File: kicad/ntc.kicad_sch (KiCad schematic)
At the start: 22 parts, among them J1 AudioJack2_SwitchT, J2 AudioJack2_SwitchT, J3 AudioJack2_SwitchT, J4 AudioJack2_SwitchT, J5 AudioJack2_SwitchT, J6 AudioJack2_SwitchT

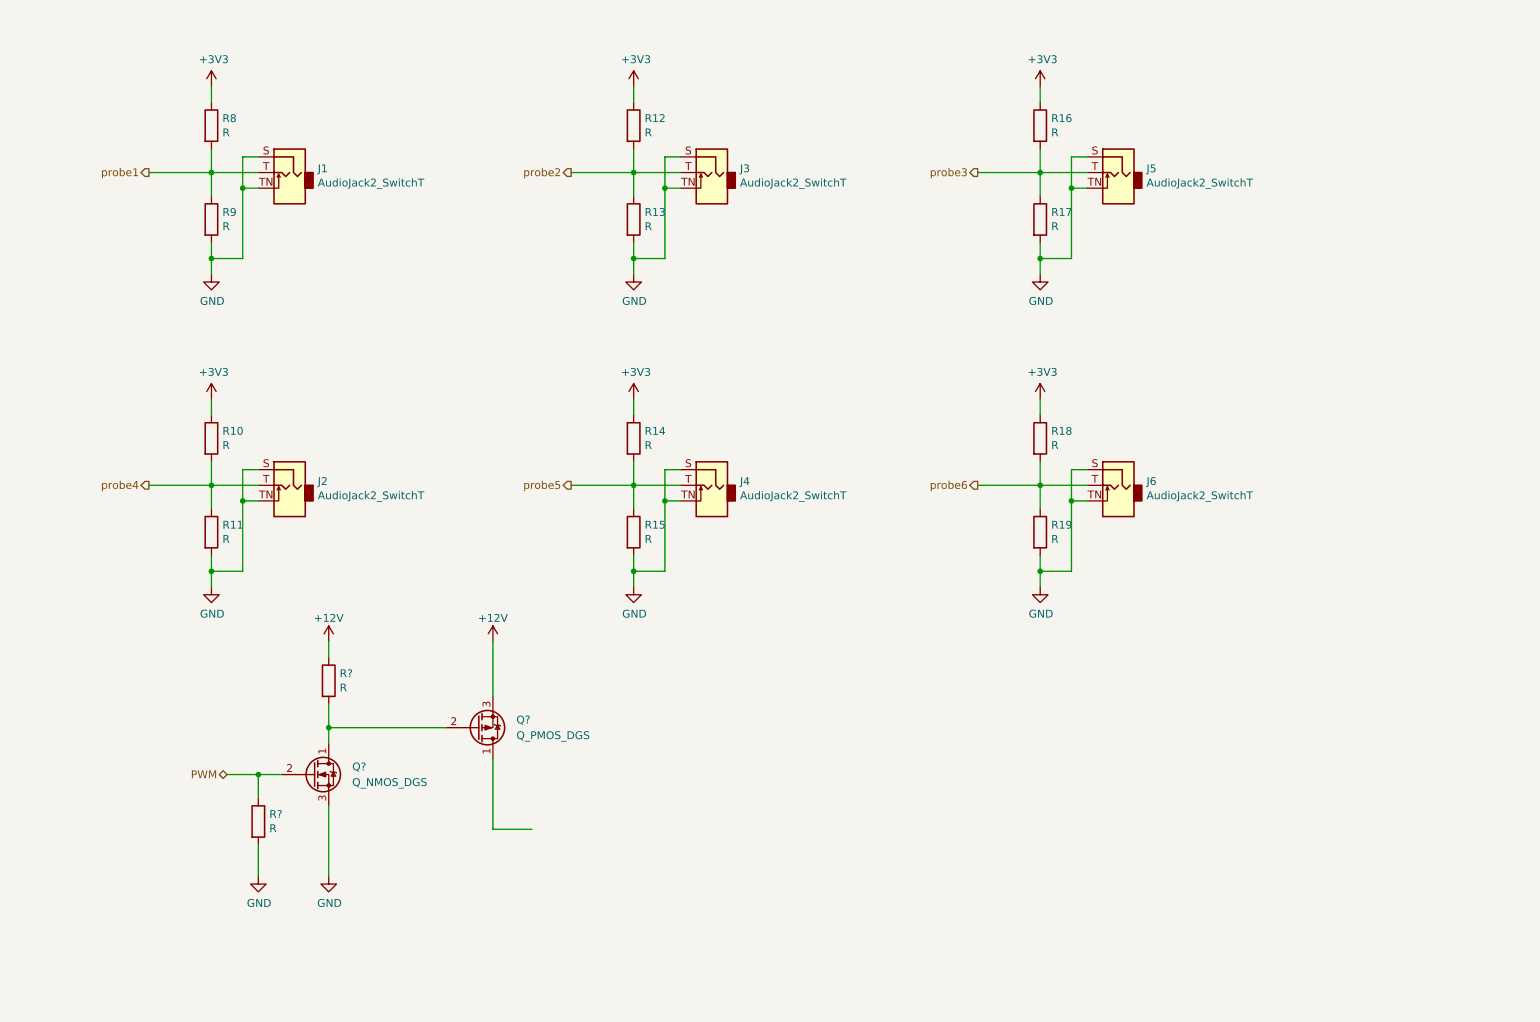
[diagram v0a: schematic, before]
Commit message: refactor KiCAD Project to v6
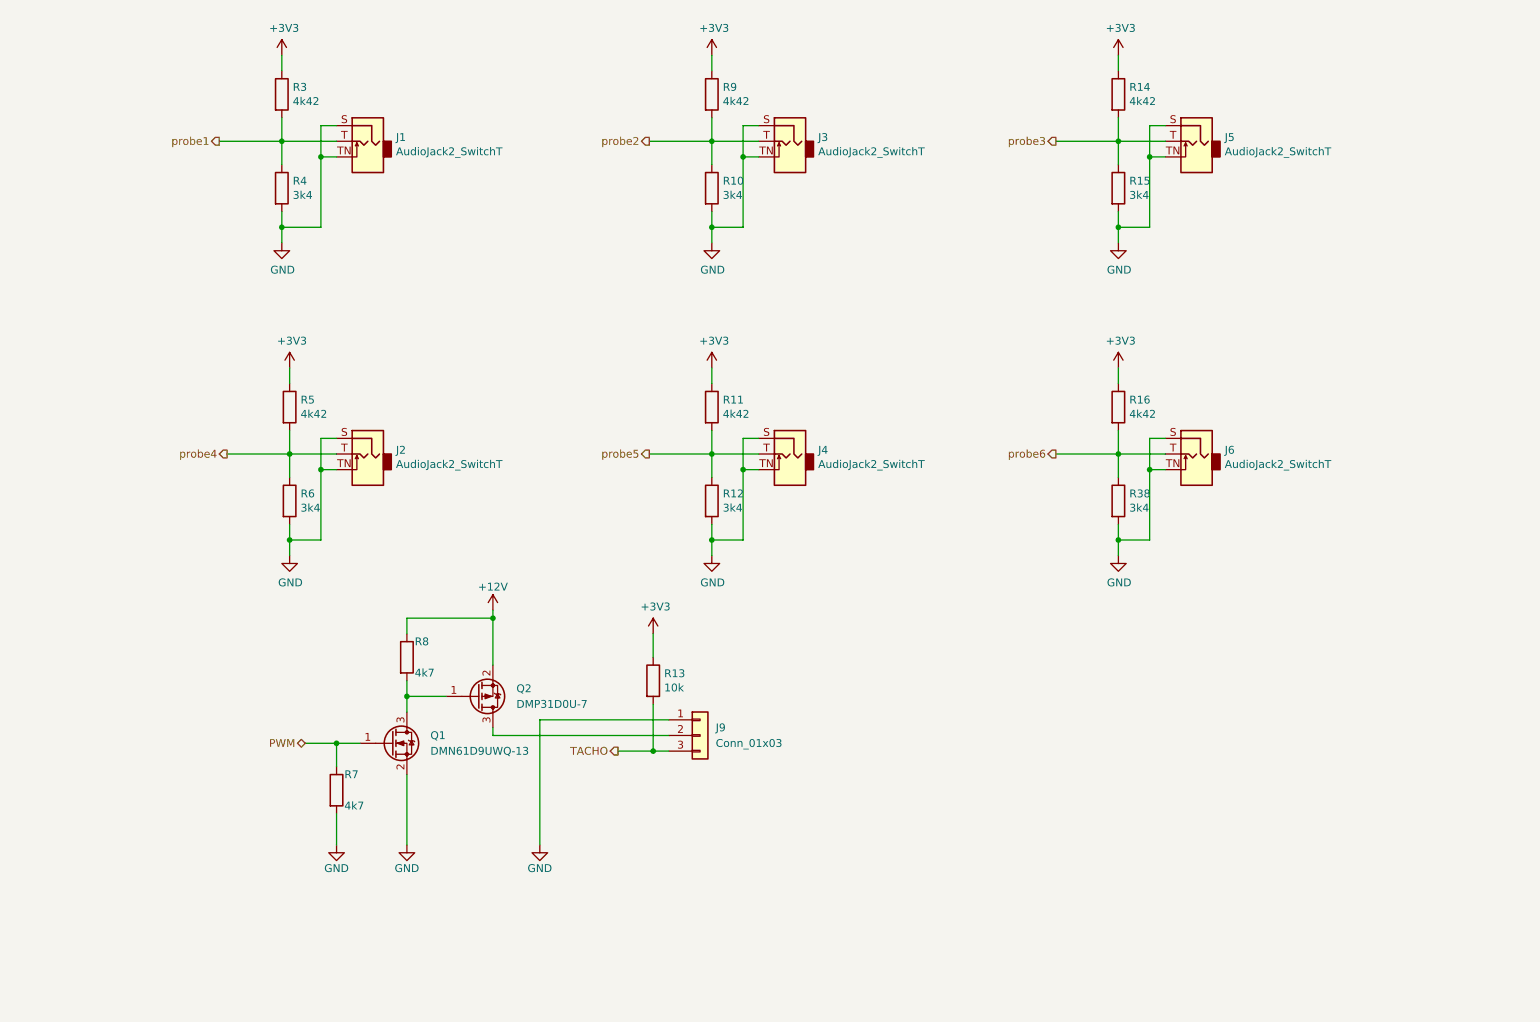
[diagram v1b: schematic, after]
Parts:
- removed Q?: Q_PMOS_DGS, symbol Device:Q_PMOS_DGS
- removed Q?: Q_NMOS_DGS, symbol Device:Q_NMOS_DGS
- removed R17, R18, R19, R? (x2): R, Resistor_SMD:R_0603_1608Metric, symbol Device:R
- added J9: Conn_01x03, z_connector:Molex_KK-254_AE-6410-03A_1x03_P2.54mm_Vertical, symbol Connector_Generic:Conn_01x03
- added Q1: DMN61D9UWQ-13, Package_TO_SOT_SMD:SOT-323_SC-70, symbol Device:Q_NMOS_GSD
- added Q2: DMP31D0U-7, Package_TO_SOT_SMD:SOT-23, symbol Device:Q_PMOS_GSD
- added R3, R5: 4k42, Resistor_SMD:R_0603_1608Metric, symbol Device:R
- added R38, R4, R6: 3k4, Resistor_SMD:R_0603_1608Metric, symbol Device:R
- added R7: 4k7, Resistor_SMD:R_0603_1608Metric, symbol Device:R
- J1, J2, J3, J4, J5, J6: Digikey (none) -> -
- R10, R12, R15: value R -> 3k4; Digikey (none) -> 311-3.40KHRCT-ND
- R11, R14, R16, R9: value R -> 4k42; Digikey (none) -> RMCF0603FT4K42CT-ND
- R13: value R -> 10k; Digikey (none) -> A121523CT-ND
- R8: value R -> 4k7; Digikey (none) -> 311-4.70KHRCT-ND
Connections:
- net +12V: now also R8.1, Q2.2 (S)
- net +3V3: now also R11.1, R13.1, R9.1, R3.1, R5.1; no longer R10.1, R12.1, R8.1
- net GND: now also R10.2, R12.2, J9.1 (Pin_1), Q1.2 (S), R38.2, R4.2, R6.2, R7.2; no longer R11.2, R13.2, R9.2
- net PWM: now also Q1.1 (G), R7.1
- net probe1: now also R3.2, R4.1; no longer R8.2, R9.1
- net probe2: now also R10.1, R9.2; no longer R12.2, R13.1
- net probe3: now also R14.2, R15.1; no longer R16.2
- net probe4: now also R5.2, R6.1; no longer R10.2, R11.1
- net probe5: now also R11.2, R12.1; no longer R14.2, R15.1
- net probe6: now also R16.2, R38.1
- new net: J9.2 (Pin_2), Q2.3 (D)
- new net: Q1.3 (D), Q2.1 (G), R8.2
- new net TACHO: J9.3 (Pin_3), R13.2

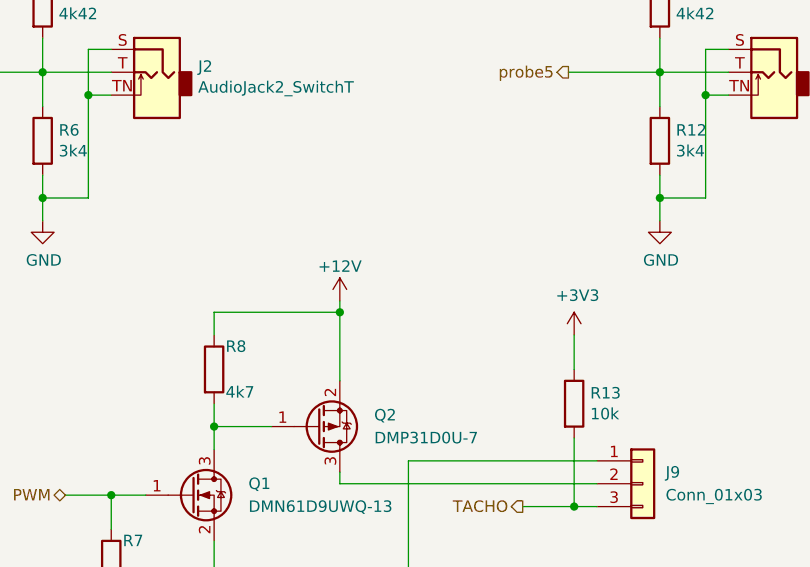
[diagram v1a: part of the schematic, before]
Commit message: add connection to lcd
import parts into pcbnew
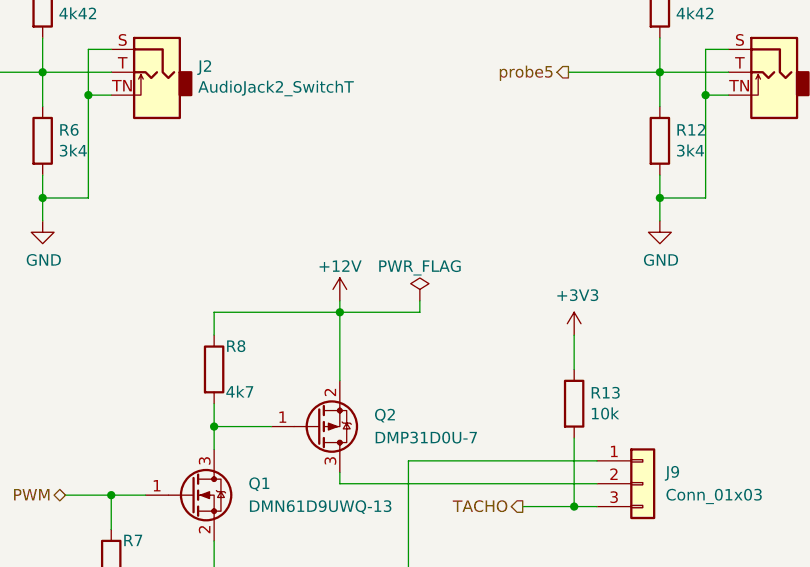
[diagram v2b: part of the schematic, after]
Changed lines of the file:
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@@
+    (stroke (width 0) (type default) (color 0 0 0 0))
+  )
+  (wire (pts (xy 115.57 127) (xy 115.57 125.73))
     (stroke (width 0) (type default) (color 0 0 0 0))
   )
@@
   )
   (wire (pts (xy 81.28 52.07) (xy 78.74 52.07))
+    (stroke (width 0) (type default) (color 0 0 0 0))
+  )
+  (wire (pts (xy 106.68 127) (xy 115.57 127))
     (stroke (width 0) (type default) (color 0 0 0 0))
   )
@@
       (effects (font (size 1.27 1.27)) hide)
     )
-    (property "Datasheet" "https://www.molex.com/pdm_docs/sd/022057038_sd.pdf" (id 3) (at 140.335 146.05 0)
+    (property "Datasheet" "~" (id 3) (at 140.335 146.05 0)
       (effects (font (size 1.27 1.27)) hide)
     )
@@
     (pin "2")
   )
+  (symbol (lib_id "power:PWR_FLAG") (at 115.57 125.73 0) (unit 1)
+    (in_bom yes) (on_board yes)
+    (property "Reference" "#FLG0103" (id 0) (at 115.57 123.825 0)
+      (effects (font (size 1.27 1.27)) hide)
+    )
+    (property "Value" "PWR_FLAG" (id 1) (at 115.57 121.92 0))
+    (property "Footprint" "" (id 2) (at 115.57 125.73 0)
+      (effects (font (size 1.27 1.27)) hide)
+    )
+    (property "Datasheet" "~" (id 3) (at 115.57 125.73 0)
+      (effects (font (size 1.27 1.27)) hide)
+    )
+    (pin "1")
+  )
   (symbol (lib_id "Connector:AudioJack2_SwitchT") (at 220.98 49.53 0) (mirror y) (unit 1)

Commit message: route complete pcb
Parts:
- renumbered J9 to J3, J3 to J4, J4 to J5, J5 to J6, J6 to J7, R9 to R10, R10 to R11, R11 to R12, R12 to R13, R38 to R17, R13 to R9
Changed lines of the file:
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@@
   (symbol (lib_id "Connector_Generic:Conn_01x03") (at 140.335 146.05 0) (unit 1)
     (in_bom yes) (on_board yes) (fields_autoplaced)
-    (property "Reference" "J9" (id 0) (at 142.875 144.7799 0)
+    (property "Reference" "J3" (id 0) (at 142.875 144.7799 0)
       (effects (font (size 1.27 1.27)) (justify left))
     )
@@
   (symbol (lib_id "Connector:AudioJack2_SwitchT") (at 154.94 49.53 0) (mirror y) (unit 1)
     (in_bom yes) (on_board yes)
-    (property "Reference" "J3" (id 0) (at 159.512 48.895 0)
+    (property "Reference" "J4" (id 0) (at 159.512 48.895 0)
       (effects (font (size 1.27 1.27)) (justify right))
     )
@@
   (symbol (lib_id "Device:R") (at 132.715 137.16 0) (unit 1)
     (in_bom yes) (on_board yes)
-    (property "Reference" "R13" (id 0) (at 134.493 135.9916 0)
+    (property "Reference" "R9" (id 0) (at 134.493 135.9916 0)
       (effects (font (size 1.27 1.27)) (justify left))
     )
@@
   (symbol (lib_id "Device:R") (at 142.24 107.95 0) (unit 1)
     (in_bom yes) (on_board yes)
-    (property "Reference" "R12" (id 0) (at 144.018 106.7816 0)
+    (property "Reference" "R13" (id 0) (at 144.018 106.7816 0)
       (effects (font (size 1.27 1.27)) (justify left))
     )
@@
   (symbol (lib_id "power:GND") (at 142.24 116.84 0) (unit 1)
     (in_bom yes) (on_board yes)
-    (property "Reference" "#PWR0112" (id 0) (at 142.24 123.19 0)
+    (property "Reference" "#PWR019" (id 0) (at 142.24 123.19 0)
       (effects (font (size 1.27 1.27)) hide)
     )
@@
   (symbol (lib_id "Device:R") (at 142.24 57.15 0) (unit 1)
     (in_bom yes) (on_board yes)
-    (property "Reference" "R10" (id 0) (at 144.018 55.9816 0)
+    (property "Reference" "R11" (id 0) (at 144.018 55.9816 0)
       (effects (font (size 1.27 1.27)) (justify left))
     )
@@
   (symbol (lib_id "power:GND") (at 92.71 163.83 0) (unit 1)
     (in_bom yes) (on_board yes)
-    (property "Reference" "#PWR0121" (id 0) (at 92.71 170.18 0)
+    (property "Reference" "#PWR012" (id 0) (at 92.71 170.18 0)
       (effects (font (size 1.27 1.27)) hide)
     )
@@
   (symbol (lib_id "power:GND") (at 114.3 163.83 0) (unit 1)
     (in_bom yes) (on_board yes)
-    (property "Reference" "#PWR0173" (id 0) (at 114.3 170.18 0)
+    (property "Reference" "#PWR014" (id 0) (at 114.3 170.18 0)
       (effects (font (size 1.27 1.27)) hide)
     )
@@
   (symbol (lib_id "Connector:AudioJack2_SwitchT") (at 154.94 100.33 0) (mirror y) (unit 1)
     (in_bom yes) (on_board yes)
-    (property "Reference" "J4" (id 0) (at 159.512 99.695 0)
+    (property "Reference" "J5" (id 0) (at 159.512 99.695 0)
       (effects (font (size 1.27 1.27)) (justify right))
     )
@@
   (symbol (lib_id "power:GND") (at 142.24 66.04 0) (unit 1)
     (in_bom yes) (on_board yes)
-    (property "Reference" "#PWR0114" (id 0) (at 142.24 72.39 0)
+    (property "Reference" "#PWR017" (id 0) (at 142.24 72.39 0)
       (effects (font (size 1.27 1.27)) hide)
     )
@@
   (symbol (lib_id "power:GND") (at 73.66 116.84 0) (unit 1)
     (in_bom yes) (on_board yes)
-    (property "Reference" "#PWR0118" (id 0) (at 73.66 123.19 0)
+    (property "Reference" "#PWR010" (id 0) (at 73.66 123.19 0)
       (effects (font (size 1.27 1.27)) hide)
     )
@@
   (symbol (lib_id "power:GND") (at 208.28 66.04 0) (unit 1)
     (in_bom yes) (on_board yes)
-    (property "Reference" "#PWR0108" (id 0) (at 208.28 72.39 0)
+    (property "Reference" "#PWR021" (id 0) (at 208.28 72.39 0)
       (effects (font (size 1.27 1.27)) hide)
     )
@@
   (symbol (lib_id "power:+3V3") (at 142.24 35.56 0) (unit 1)
     (in_bom yes) (on_board yes)
-    (property "Reference" "#PWR0111" (id 0) (at 142.24 39.37 0)
+    (property "Reference" "#PWR016" (id 0) (at 142.24 39.37 0)
       (effects (font (size 1.27 1.27)) hide)
     )
@@
   (symbol (lib_id "power:+12V") (at 106.68 125.73 0) (unit 1)
     (in_bom yes) (on_board yes)
-    (property "Reference" "#PWR0119" (id 0) (at 106.68 129.54 0)
+    (property "Reference" "#PWR013" (id 0) (at 106.68 129.54 0)
       (effects (font (size 1.27 1.27)) hide)
     )
@@
   (symbol (lib_id "Connector:AudioJack2_SwitchT") (at 220.98 100.33 0) (mirror y) (unit 1)
     (in_bom yes) (on_board yes)
-    (property "Reference" "J6" (id 0) (at 225.552 99.695 0)
+    (property "Reference" "J7" (id 0) (at 225.552 99.695 0)
       (effects (font (size 1.27 1.27)) (justify right))
     )
@@
   (symbol (lib_id "power:+3V3") (at 142.24 86.36 0) (unit 1)
     (in_bom yes) (on_board yes)
-    (property "Reference" "#PWR0113" (id 0) (at 142.24 90.17 0)
+    (property "Reference" "#PWR018" (id 0) (at 142.24 90.17 0)
       (effects (font (size 1.27 1.27)) hide)
     )
@@
   (symbol (lib_id "power:GND") (at 208.28 116.84 0) (unit 1)
     (in_bom yes) (on_board yes)
-    (property "Reference" "#PWR0110" (id 0) (at 208.28 123.19 0)
+    (property "Reference" "#PWR023" (id 0) (at 208.28 123.19 0)
       (effects (font (size 1.27 1.27)) hide)
     )
@@
   (symbol (lib_id "Device:R") (at 208.28 107.95 0) (unit 1)
     (in_bom yes) (on_board yes)
-    (property "Reference" "R38" (id 0) (at 210.058 106.7816 0)
+    (property "Reference" "R17" (id 0) (at 210.058 106.7816 0)
       (effects (font (size 1.27 1.27)) (justify left))
     )
@@
   (symbol (lib_id "power:+3V3") (at 72.39 35.56 0) (unit 1)
     (in_bom yes) (on_board yes)
-    (property "Reference" "#PWR0115" (id 0) (at 72.39 39.37 0)
+    (property "Reference" "#PWR07" (id 0) (at 72.39 39.37 0)
       (effects (font (size 1.27 1.27)) hide)
     )
@@
   (symbol (lib_id "power:+3V3") (at 73.66 86.36 0) (unit 1)
     (in_bom yes) (on_board yes)
-    (property "Reference" "#PWR0116" (id 0) (at 73.66 90.17 0)
+    (property "Reference" "#PWR09" (id 0) (at 73.66 90.17 0)
       (effects (font (size 1.27 1.27)) hide)
     )
@@
   (symbol (lib_id "power:PWR_FLAG") (at 115.57 125.73 0) (unit 1)
     (in_bom yes) (on_board yes)
-    (property "Reference" "#FLG0103" (id 0) (at 115.57 123.825 0)
+    (property "Reference" "#FLG03" (id 0) (at 115.57 123.825 0)
       (effects (font (size 1.27 1.27)) hide)
     )
@@
   (symbol (lib_id "Connector:AudioJack2_SwitchT") (at 220.98 49.53 0) (mirror y) (unit 1)
     (in_bom yes) (on_board yes)
-    (property "Reference" "J5" (id 0) (at 225.552 48.895 0)
+    (property "Reference" "J6" (id 0) (at 225.552 48.895 0)
       (effects (font (size 1.27 1.27)) (justify right))
     )
@@
   (symbol (lib_id "Device:R") (at 142.24 92.71 0) (unit 1)
     (in_bom yes) (on_board yes)
-    (property "Reference" "R11" (id 0) (at 144.018 91.5416 0)
+    (property "Reference" "R12" (id 0) (at 144.018 91.5416 0)
       (effects (font (size 1.27 1.27)) (justify left))
     )
@@
   (symbol (lib_id "Device:R") (at 142.24 41.91 0) (unit 1)
     (in_bom yes) (on_board yes)
-    (property "Reference" "R9" (id 0) (at 144.018 40.7416 0)
+    (property "Reference" "R10" (id 0) (at 144.018 40.7416 0)
       (effects (font (size 1.27 1.27)) (justify left))
     )
@@
   (symbol (lib_id "power:+3V3") (at 132.715 129.54 0) (unit 1)
     (in_bom yes) (on_board yes)
-    (property "Reference" "#PWR02" (id 0) (at 132.715 133.35 0)
+    (property "Reference" "#PWR015" (id 0) (at 132.715 133.35 0)
       (effects (font (size 1.27 1.27)) hide)
     )
@@
   (symbol (lib_id "power:GND") (at 72.39 66.04 0) (unit 1)
     (in_bom yes) (on_board yes)
-    (property "Reference" "#PWR0117" (id 0) (at 72.39 72.39 0)
+    (property "Reference" "#PWR08" (id 0) (at 72.39 72.39 0)
       (effects (font (size 1.27 1.27)) hide)
     )
@@
   (symbol (lib_id "power:+3V3") (at 208.28 35.56 0) (unit 1)
     (in_bom yes) (on_board yes)
-    (property "Reference" "#PWR0107" (id 0) (at 208.28 39.37 0)
+    (property "Reference" "#PWR020" (id 0) (at 208.28 39.37 0)
       (effects (font (size 1.27 1.27)) hide)
     )
@@
   (symbol (lib_id "power:+3V3") (at 208.28 86.36 0) (unit 1)
     (in_bom yes) (on_board yes)
-    (property "Reference" "#PWR0109" (id 0) (at 208.28 90.17 0)
+    (property "Reference" "#PWR022" (id 0) (at 208.28 90.17 0)
       (effects (font (size 1.27 1.27)) hide)
     )
@@
   (symbol (lib_id "power:GND") (at 81.28 163.83 0) (unit 1)
     (in_bom yes) (on_board yes)
-    (property "Reference" "#PWR0120" (id 0) (at 81.28 170.18 0)
-      (effects (font (size 1.27 1.27)) hide)
-    )
+    (property "Reference" "#PWR011" (id 0) (at 81.28 170.18 0)
+      (effects (font (size 1.27 1.27)) hide)
+    )

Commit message: rework pcb
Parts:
- J1, J2, J4, J5, J6, J7: footprint z_connector:MJ-2523 -> mylib_connector:MJ-2523
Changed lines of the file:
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@@
       (effects (font (size 1.27 1.27)) (justify right))
     )
-    (property "Footprint" "z_connector:MJ-2523" (id 2) (at 154.94 49.53 0)
+    (property "Footprint" "mylib_connector:MJ-2523" (id 2) (at 154.94 49.53 0)
       (effects (font (size 1.27 1.27)) hide)
     )
@@
       (effects (font (size 1.27 1.27)) (justify right))
     )
-    (property "Footprint" "z_connector:MJ-2523" (id 2) (at 154.94 100.33 0)
+    (property "Footprint" "mylib_connector:MJ-2523" (id 2) (at 154.94 100.33 0)
       (effects (font (size 1.27 1.27)) hide)
     )
@@
       (effects (font (size 1.27 1.27)) (justify right))
     )
-    (property "Footprint" "z_connector:MJ-2523" (id 2) (at 86.36 100.33 0)
+    (property "Footprint" "mylib_connector:MJ-2523" (id 2) (at 86.36 100.33 0)
       (effects (font (size 1.27 1.27)) hide)
     )
@@
       (effects (font (size 1.27 1.27)) (justify right))
     )
-    (property "Footprint" "z_connector:MJ-2523" (id 2) (at 220.98 100.33 0)
+    (property "Footprint" "mylib_connector:MJ-2523" (id 2) (at 220.98 100.33 0)
       (effects (font (size 1.27 1.27)) hide)
     )
@@
       (effects (font (size 1.27 1.27)) (justify right))
     )
-    (property "Footprint" "z_connector:MJ-2523" (id 2) (at 86.36 49.53 0)
+    (property "Footprint" "mylib_connector:MJ-2523" (id 2) (at 86.36 49.53 0)
       (effects (font (size 1.27 1.27)) hide)
     )
@@
       (effects (font (size 1.27 1.27)) (justify right))
     )
-    (property "Footprint" "z_connector:MJ-2523" (id 2) (at 220.98 49.53 0)
-      (effects (font (size 1.27 1.27)) hide)
-    )
+    (property "Footprint" "mylib_connector:MJ-2523" (id 2) (at 220.98 49.53 0)
+      (effects (font (size 1.27 1.27)) hide)
+    )
